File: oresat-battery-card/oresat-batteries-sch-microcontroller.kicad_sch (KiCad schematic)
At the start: 40 parts, among them J2 SM14B-SHLS-TF, U20 TCAN330G, U7 MCXN947VKLT, Y2 24 MHz

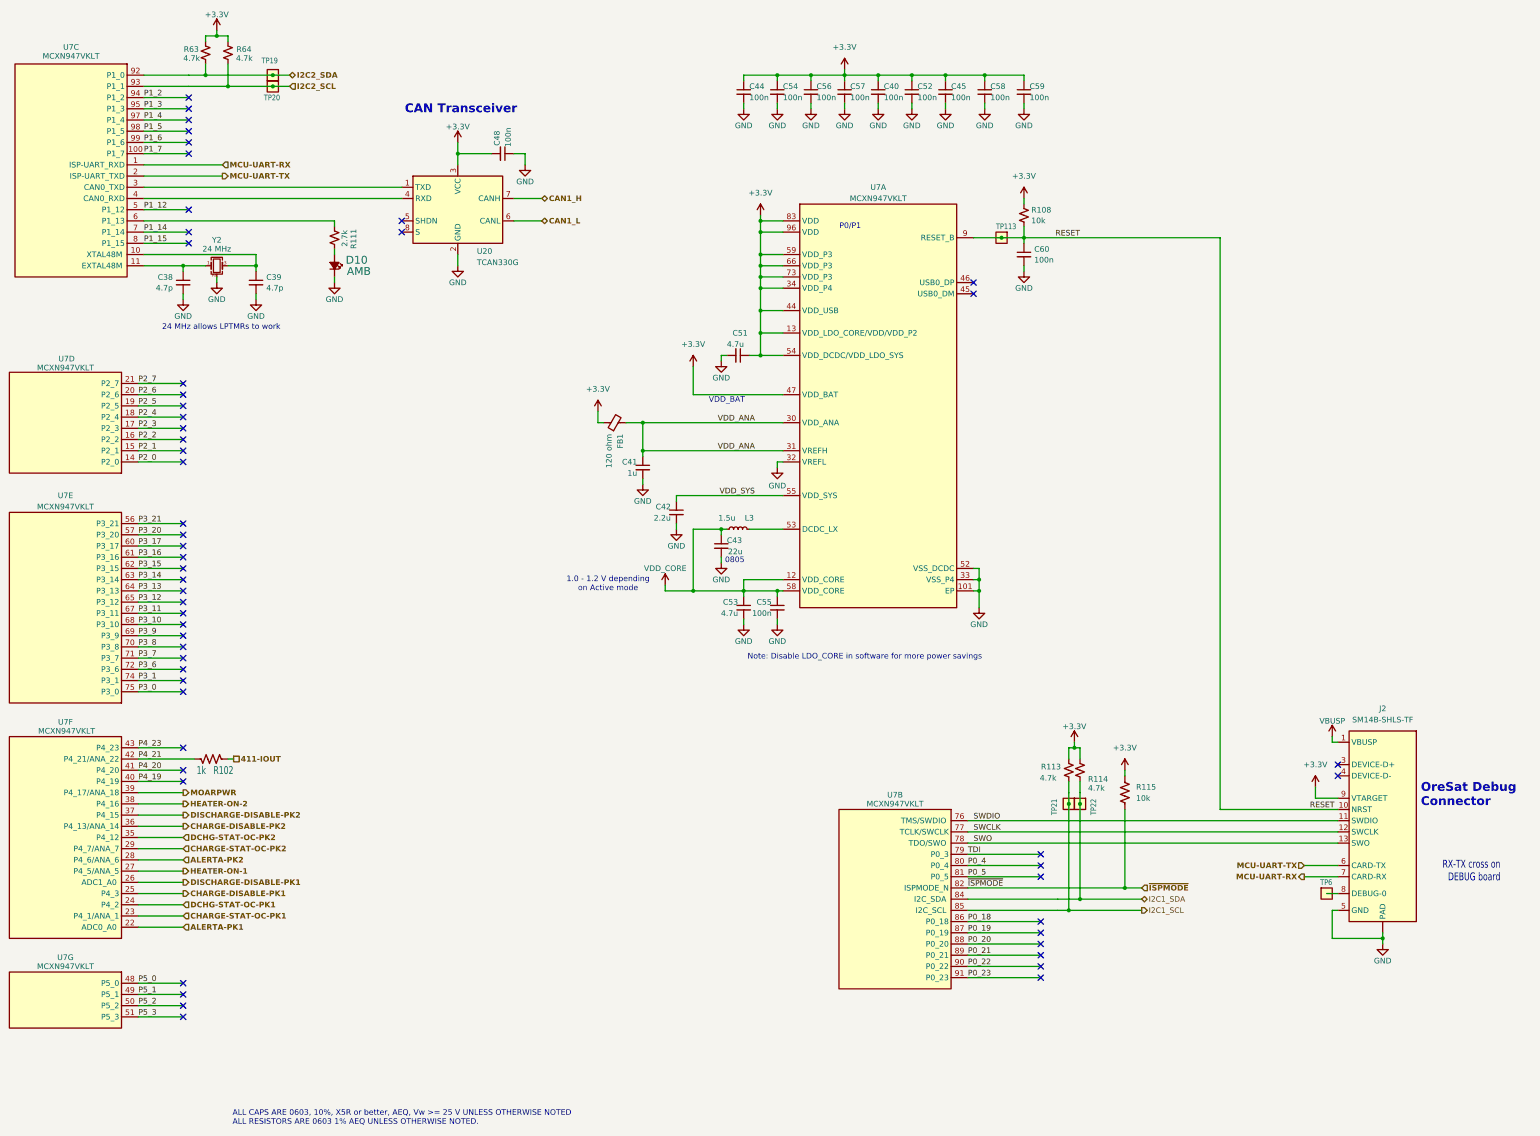
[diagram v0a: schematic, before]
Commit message: Jumped back on the TPS bandwagon - LCSC to the rescue! - and lots of cleanup.
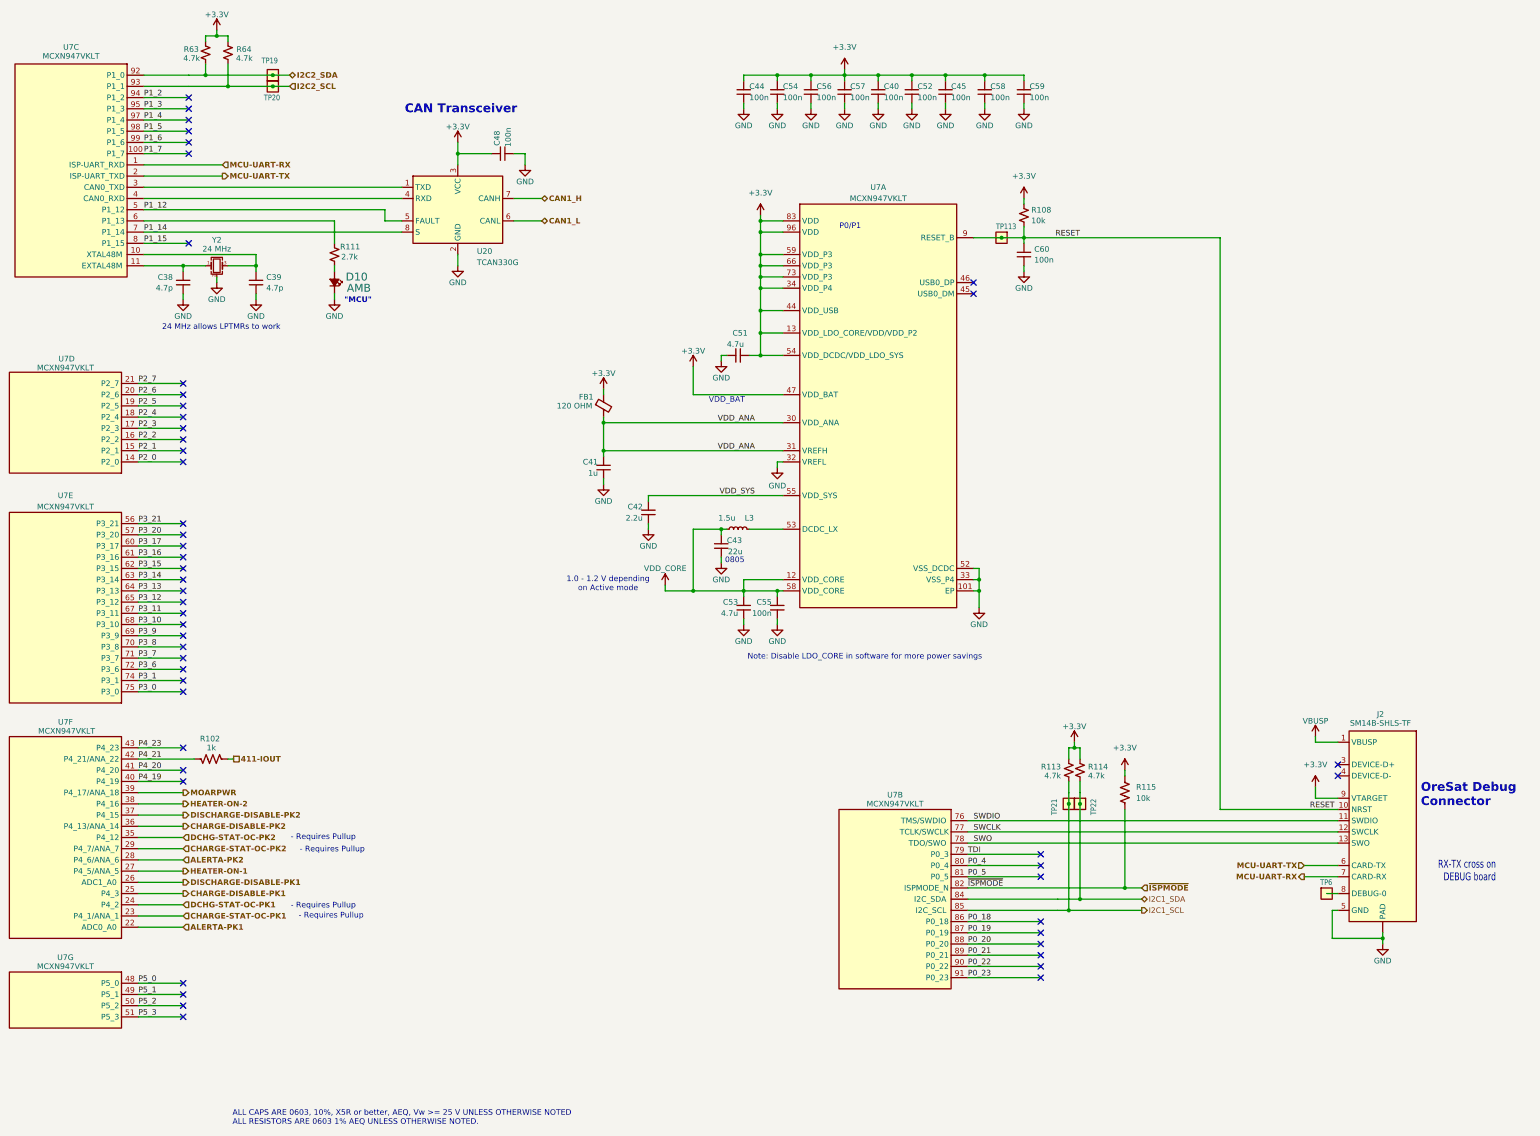
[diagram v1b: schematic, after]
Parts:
- FB1: value 120 ohm -> 120 OHM
- R102: DPN RMCF0603FT2K70CT-ND -> RMCF0603FT1K00CT-ND
- U20: symbol Interface_CAN_LIN:TCAN330G -> Interface_CAN_LIN:TCAN337G
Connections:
- net P1_12: now also U20.5 (FAULT)
- net P1_14: now also U20.8 (S)
- no-connect marks 55 -> 51
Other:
- note added: ""MCU""
- note added: "- Requires Pullup"
- moved on the sheet: C41, C42, D10, FB1, R111

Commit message: Battery Card 4.0, no ERC or DRC errors or warnings
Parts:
- C51, C53: footprint oresat-passives:0603-C-NOSILK -> oresat-passives:0805-C-NOSILK; DPN 490-GRT188C71C475KE13DCT-ND -> 490-GRT21BC71E475KE13LCT-ND; MPN GRT188C71C475KE13D -> GRT21BC71E475KE13L
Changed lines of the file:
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@@
 	(title_block
 		(title "OreSat Battery Card")
-		(date "2026-09-27")
+		(date "2026-10-06")
 		(rev "4.0")
 		(company "Portland State Aerospace Society")
@@
 			)
 		)
-		(property "Footprint" "oresat-passives:0603-C-NOSILK"
+		(property "Footprint" "oresat-passives:0805-C-NOSILK"
 			(at 228.6 148.59 0)
 			(hide yes)
@@
 			)
 		)
-		(property "Datasheet" "https://search.murata.co.jp/Ceramy/image/img/A01X/G101/ENG/GRT188C71C475KE13-01.pdf"
+		(property "Datasheet" "https://search.murata.co.jp/Ceramy/image/img/A01X/G101/ENG/GRT21BC71E475KE13-01.pdf"
 			(at 228.6 148.59 0)
 			(hide yes)
@@
 			)
 		)
-		(property "Description" "4.7 µF ±10% 16V Ceramic Capacitor X7S 0603 (1608 Metric)"
+		(property "Description" "4.7 µF ±10% 25V Ceramic Capacitor X7S 0805 (2012 Metric)"
 			(at 228.6 148.59 0)
 			(hide yes)
@@
 			)
 		)
-		(property "MPN" "GRT188C71C475KE13D"
+		(property "MPN" "GRT21BC71E475KE13L"
 			(at 228.6 148.59 0)
 			(hide yes)
@@
 			)
 		)
-		(property "DPN" "490-GRT188C71C475KE13DCT-ND"
+		(property "DPN" "490-GRT21BC71E475KE13LCT-ND"
 			(at 228.6 148.59 0)
 			(hide yes)
@@
 			)
 		)
-		(property "Footprint" "oresat-passives:0603-C-NOSILK"
+		(property "Footprint" "oresat-passives:0805-C-NOSILK"
 			(at 227.33 91.44 0)
 			(hide yes)
@@
 			)
 		)
-		(property "Datasheet" "https://search.murata.co.jp/Ceramy/image/img/A01X/G101/ENG/GRT188C71C475KE13-01.pdf"
+		(property "Datasheet" "https://search.murata.co.jp/Ceramy/image/img/A01X/G101/ENG/GRT21BC71E475KE13-01.pdf"
 			(at 227.33 91.44 0)
 			(hide yes)
@@
 			)
 		)
-		(property "Description" "4.7 µF ±10% 16V Ceramic Capacitor X7S 0603 (1608 Metric)"
+		(property "Description" "4.7 µF ±10% 25V Ceramic Capacitor X7S 0805 (2012 Metric)"
 			(at 227.33 91.44 0)
 			(hide yes)
@@
 			)
 		)
-		(property "MPN" "GRT188C71C475KE13D"
+		(property "MPN" "GRT21BC71E475KE13L"
 			(at 227.33 91.44 0)
 			(hide yes)
@@
 			)
 		)
-		(property "DPN" "490-GRT188C71C475KE13DCT-ND"
+		(property "DPN" "490-GRT21BC71E475KE13LCT-ND"
 			(at 227.33 91.44 90)
 			(hide yes)

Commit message: Updated Makefile and Readme; fixed TCAN IC, cleanup, fix battery connections that were killed somehow
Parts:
- added TP27, TP29, TP34: TEST-POINT-LARGE-SQUARE, oresat-misc:TestPoint-0.75mm-th, symbol oresat-misc:Test-Point-0.75mm-th
- U20: value TCAN330G -> TCAN337G; DPN 296-44211-1-ND -> TCAN337GD-ND; MPN TCAN330GDCNT -> TCAN337GD
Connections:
- net P0_21 is gone; now on net GND: U7.89 (P0_21)
- net P0_22 is gone; now on net GND: U7.90 (P0_22)
- net P0_23 is gone; now on net GND: U7.91 (P0_23)
- net P1_7: now also TP29.1
- net P3_8: now also TP27.1
- net P5_3: now also TP34.1
- net TDI  renamed P0_3
- no-connect marks 51 -> 45
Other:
- note added: "Hardware version number (use pullups)"
- note added: "Rev: 000"

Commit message: Changes to eFuse after trying evaluation board, and recalculating values, and trying to reduce number of passive components to minimum number
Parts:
- R108, R115: MFR Stackpole Electronics Inc -> Stackpole Electronics
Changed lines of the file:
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@@
 			)
 		)
-		(property "MFR" "Stackpole Electronics Inc"
+		(property "MFR" "Stackpole Electronics"
 			(at 292.1 59.69 0)
 			(hide yes)
@@
 			)
 		)
-		(property "MFR" "Stackpole Electronics Inc"
+		(property "MFR" "Stackpole Electronics"
 			(at 314.96 190.5 90)
 			(hide yes)

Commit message: Added imon capabilities, cleaned up some lingering DRCs that kept popping back up.
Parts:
- removed TP34: TEST-POINT-LARGE-SQUARE, oresat-misc:TestPoint-0.75mm-th, symbol oresat-misc:Test-Point-0.75mm-th
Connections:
- net P5_2 renamed IMON-PK1
- net P5_3 renamed IMON-PK2
- no-connect marks 45 -> 44
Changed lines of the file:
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@@
 	)
 	(no_connect
-		(at 101.6 187.96)
-	)
-	(no_connect
 		(at 363.22 184.15)
 	)
@@
 	)
 	(no_connect
-		(at 101.6 238.76)
-	)
-	(no_connect
 		(at 101.6 107.95)
 	)
@@
 	)
 	(no_connect
+		(at 101.6 187.96)
+	)
+	(no_connect
 		(at 101.6 105.41)
 	)
@@
 	(wire
 		(pts
-			(xy 91.44 241.3) (xy 105.41 241.3)
+			(xy 91.44 241.3) (xy 101.6 241.3)
 		)
 		(stroke
@@
 	(wire
 		(pts
-			(xy 91.44 187.96) (xy 101.6 187.96)
-		)
-		(stroke
-			(width 0)
-			(type default)
-		)
-	)
-	(wire
-		(pts
 			(xy 232.41 59.69) (xy 232.41 60.96)
 		)
@@
 	(wire
 		(pts
+			(xy 91.44 187.96) (xy 101.6 187.96)
+		)
+		(stroke
+			(width 0)
+			(type default)
+		)
+	)
+	(wire
+		(pts
 			(xy 232.41 76.2) (xy 232.41 73.66)
 		)
@@
 		)
 	)
-	(label "P1_14"
-		(at 92.71 63.5 0)
+	(label "P4_19"
+		(at 91.44 187.96 0)
 		(effects
 			(font
@@
 		)
 	)
-	(label "~{ISPMODE}"
-		(at 279.4 212.09 0)
+	(label "P1_14"
+		(at 92.71 63.5 0)
 		(effects
 			(font
@@
 		)
 	)
-	(label "P0_19"
-		(at 279.4 222.25 0)
+	(label "~{ISPMODE}"
+		(at 279.4 212.09 0)
 		(effects
 			(font
@@
 		)
 	)
-	(label "P4_19"
-		(at 91.44 187.96 0)
+	(label "P0_19"
+		(at 279.4 222.25 0)
 		(effects
 			(font
@@
 		)
 	)
-	(label "P4_20"
-		(at 91.44 185.42 0)
-		(effects
-			(font
-				(size 1.27 1.27)
-			)
-			(justify left bottom)
-		)
-	)
 	(label "P3_11"
 		(at 91.44 149.86 0)
@@
 		)
 	)
+	(label "P4_20"
+		(at 91.44 185.42 0)
+		(effects
+			(font
+				(size 1.27 1.27)
+			)
+			(justify left bottom)
+		)
+	)
 	(label "VDD_ANA"
 		(at 231.14 113.03 180)
@@
 		)
 	)
-	(label "P5_3"
-		(at 91.44 241.3 0)
-		(effects
-			(font
-				(size 1.27 1.27)
-			)
-			(justify left bottom)
-		)
-	)
 	(label "VDD_SYS"
 		(at 231.14 123.19 180)
@@
 		)
 	)
-	(label "P5_2"
-		(at 91.44 238.76 0)
-		(effects
-			(font
-				(size 1.27 1.27)
-			)
-			(justify left bottom)
-		)
-	)
 	(label "P3_15"
 		(at 91.44 139.7 0)
@@
 		)
 	)
+	(hierarchical_label "IMON-PK1"
+		(shape input)
+		(at 101.6 238.76 0)
+		(effects
+			(font
+				(size 1.27 1.27)
+				(thickness 0.254)
+				(bold yes)
+			)
+			(justify left)
+		)
+	)
+	(hierarchical_label "IMON-PK2"
+		(shape input)
+		(at 101.6 241.3 0)
+		(effects
+			(font
+				(size 1.27 1.27)
+				(thickness 0.254)
+				(bold yes)
+			)
+			(justify left)
+		)
+	)
 	(symbol
 		(lib_id "power:+3.3V")
@@
 		)
 		(pin "50"
+			(alternate "ADC1_B10")
 		)
 		(pin "51"
+			(alternate "ADC1_B11")
 		)
 		(pin "38"
@@
 					(unit 1)
 				)
-			)
-		)
-	)
-	(symbol
-		(lib_id "oresat-misc:Test-Point-0.75mm-th")
-		(at 105.41 241.3 270)
-		(mirror x)
-		(unit 1)
-		(body_style 1)
-		(exclude_from_sim yes)
-		(in_bom no)
-		(on_board yes)
-		(in_pos_files yes)
-		(dnp no)
-		(property "Reference" "TP34"
-			(at 103.378 239.776 90)
-			(show_name no)
-			(do_not_autoplace no)
-			(effects
-				(font
-					(size 1.27 1.0795)
-				)
-				(justify left top)
-			)
-		)
-		(property "Value" "TEST-POINT-LARGE-SQUARE"
-			(at 105.41 241.3 0)
-			(hide yes)
-			(show_name no)
-			(do_not_autoplace no)
-			(effects
-				(font
-					(size 1.27 1.27)
-				)
-			)
-		)
-		(property "Footprint" "oresat-misc:TestPoint-0.75mm-th"
-			(at 115.57 241.3 0)
-			(hide yes)
-			(show_name no)
-			(do_not_autoplace no)
-			(effects
-				(font
-					(size 1.27 1.27)
-				)
-			)
-		)
-		(property "Datasheet" ""
-			(at 105.41 241.3 0)
-			(hide yes)
-			(show_name no)
-			(do_not_autoplace no)
-			(effects
-				(font
-					(size 1.27 1.27)
-				)
-			)
-		)
-		(property "Description" "0.75 mm TH test point; good for scope probes and jumpers"
-			(at 105.41 241.3 0)
-			(hide yes)
-			(show_name no)
-			(do_not_autoplace no)
-			(effects
-				(font
-					(size 1.27 1.27)
-				)
-			)
-		)
-		(pin "1"
-		)
-		(instances
-			(project "oresat-batteries"
-				(path "/d5070776-2522-4f7b-9d31-10770161e48a/60cc160f-89b6-42ae-bb0a-7f727f347e07"
-					(reference "TP34")
-					(unit 1)
-				)

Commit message: Fix CAN trasnceiver part number
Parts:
- U20: value TCAN337G -> TCAN337GDCN; DPN TCAN337GD-ND -> 296-44539-1-ND; MPN TCAN337GD -> TCAN337GDCNT
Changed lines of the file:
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@@
 			)
 		)
-		(property "Value" "TCAN337G"
+		(property "Value" "TCAN337GDCN"
 			(at 168.148 71.12 0)
 			(show_name no)
@@
 			)
 		)
-		(property "Description" "1/1 Transceiver Half CANbus 8-SOIC"
+		(property "Description" "1/1 Transceiver Half CANbus SOT-23-8"
 			(at 163.83 58.42 0)
 			(hide yes)
@@
 			)
 		)
-		(property "DPN" "TCAN337GD-ND"
+		(property "DPN" "296-44539-1-ND"
 			(at 163.83 58.42 0)
 			(hide yes)
@@
 			)
 		)
-		(property "MPN" "TCAN337GD"
+		(property "MPN" "TCAN337GDCNT"
 			(at 163.83 58.42 0)
 			(hide yes)
